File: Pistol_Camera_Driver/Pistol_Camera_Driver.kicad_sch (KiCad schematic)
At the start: 118 parts, among them J1 Screw_Terminal_01x02, J10 I2C, J11 Screw_Terminal_01x02, J12 Screw_Terminal_01x02, J13 I2C, J14 Screw_Terminal_01x02, J15 Screw_Terminal_01x02, J16 Screw_Terminal_01x02, J17 Screw_Terminal_01x02, J19 I2C, J2 Objective, J3 Screw_Terminal_01x02, J4 Screw_Terminal_01x02, J5 Screw_Terminal_01x02, J6 Joystick, J7 Screw_Terminal_01x02, J8 Screw_Terminal_01x02, J9 Screw_Terminal_01x02, M1 Fan, U1 XL1509-3.3, U12 MT3608, U2 XL1509-5.0, U4 DRV8834PWP, U5 DRV8834PWP

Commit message: v0.2 circuit was completed
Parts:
- removed C20, C22: 22u, Capacitor_SMD:C_0603_1608Metric_Pad1.08x0.95mm_HandSolder, symbol Device:C
- removed C21, C24: 0.1, Capacitor_SMD:C_0603_1608Metric_Pad1.08x0.95mm_HandSolder, symbol Device:C
- removed D1, D9: UV_LED, symbol Device:LED
- removed D2, D4, D6: CDBA3100-HF, Diode_SMD:D_SMA, symbol Diode:CDBA3100-HF
- removed D3: WHITE_LED, symbol Device:LED
- removed D5: RED_LED, symbol Device:LED
- removed R14, R15, R16, R18, R20, R21, R22, R23, R24, R25, R26, R27, R28, R29, R30, R31, R32, R33, R34, R35, R36, R37, R38, R39: 1, Resistor_SMD:R_0603_1608Metric_Pad0.98x0.95mm_HandSolder, symbol Device:R
- removed U6, U7, U8, U9: ~, Package_SO:PowerIntegrations_SO-8, symbol Vedro:LED2000DR
- added R42, R43, R44, R45: 10k, Resistor_SMD:R_0603_1608Metric_Pad0.98x0.95mm_HandSolder, symbol Device:R
- added R46, R47, R48, R49, R52, R53, R54, R55: 1, Resistor_SMD:R_0603_1608Metric_Pad0.98x0.95mm_HandSolder, symbol Device:R
- added U11, U13, U14, U15: ~, Package_TO_SOT_SMD:SOT-89-5_Handsoldering, symbol myLib8_sym:BP1361
- added VD1, VD2, VD3, VD4, VD5, VD6, VD7: CDBA3100-HF, Diode_SMD:D_SOD-123, symbol Diode:CDBA3100-HF
- C13, C15, C16, C17, C19, C3: footprint Capacitor_SMD:C_0603_1608Metric_Pad1.08x0.95mm_HandSolder -> Capacitor_SMD:C_0805_2012Metric_Pad1.18x1.45mm_HandSolder
- C14, C18: value 0.1 -> 22u; footprint Capacitor_SMD:C_0603_1608Metric_Pad1.08x0.95mm_HandSolder -> Capacitor_SMD:C_0805_2012Metric_Pad1.18x1.45mm_HandSolder
- L1, L2, L3, L4: value 4u7 -> 47uH; footprint Inductor_SMD:L_Chilisin_BMRx00040412 -> Inductor_SMD:L_APV_ANR5045
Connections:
- net +3.3VP: now also VD7.1 (K)
- net +5V: now also VD6.1 (K)
- net EP: now also C17.1, C19.1, C3.1, R42.2, R43.2, R44.2, R45.2, U11.2 (GND), U13.2 (GND), U14.2 (GND), U15.2 (GND), VD6.2 (A), VD7.2 (A); no longer C13.2, C15.2, C16.2, C17.2, C18.1, C19.2, C3.2
- net PWM_IR: now also R45.1, U15.3 (DIM)
- net PWM_RED: now also R43.1, U13.3 (DIM)
- net PWM_UV: now also R44.1, U14.3 (DIM)
- net PWM_WHITE: now also R42.1, U11.3 (DIM)
- net VPP: now also C17.2, C19.2, C3.2, R46.1, R47.1, R48.1, R49.1, R52.1, R53.1, R54.1, R55.1, U11.5 (VIN), U13.5 (VIN), U14.1 (CS), U14.5 (VIN), U15.5 (VIN), VD1.1 (K), VD2.1 (K), VD3.1 (K), VD4.1 (K), VD5.1 (K); no longer C15.1, C16.1, C18.2, C19.1
- net at J12.2 (Pin_2): now also C18.2, L2.2
- net at L2.1: now also U15.4 (SW), VD4.2 (A)
- net at Je1.2 (Pin_2): now also C13.2, L4.2
- net at J9.2 (Pin_2): now also C16.2, L3.2
- net at L4.1: now also U11.4 (SW), VD1.2 (A)
- net at J12.1 (Pin_1): now also C18.1, R54.2, R55.2, U15.1 (CS); no longer L4.2
- net at L7.2, U12.1 (SW): now also VD5.2 (A)
- net at J7.2 (Pin_2): now also C15.2, L1.2
- net at L1.1: now also U13.4 (SW), VD2.2 (A)
- net at L3.1: now also U14.4 (SW), VD3.2 (A)
- new net: C13.1, Je1.1 (Pin_1), R46.2, R47.2, U11.1 (CS)
- new net: C16.1, J9.1 (Pin_1), R52.2, R53.2
- new net: C15.1, J7.1 (Pin_1), R48.2, R49.2, U13.1 (CS)

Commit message: v0.3 actual state
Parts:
- removed C23: 470uF, Capacitor_SMD:CP_Elec_10x10.5, symbol Device:C_Polarized
- removed C26: 180uF, Capacitor_SMD:CP_Elec_6.3x7.7, symbol Device:C_Polarized
- removed Je1: Screw_Terminal_01x02, Connector_PinSocket_2.54mm:PinSocket_1x02_P2.54mm_Vertical, symbol Connector:Screw_Terminal_01x02
- removed U13, U14, U15: ~, Package_TO_SOT_SMD:SOT-89-5_Handsoldering, symbol myLib8_sym:BP1361
- added C20: 470uF, Capacitor_THT:CP_Radial_D8.0mm_P3.50mm, symbol Device:C_Polarized
- added C21: 330uF, Capacitor_THT:CP_Radial_D8.0mm_P3.50mm, symbol Device:C_Polarized
- added J18: Screw_Terminal_01x02, Connector_JST:JST_XH_B2B-XH-A_1x02_P2.50mm_Vertical, symbol Connector:Screw_Terminal_01x02
- added R14, R15, R16, R18, R20, R21, R22, R23, R24, R25, R26, R27, R28, R29, R30, R31: 1, Resistor_SMD:R_0603_1608Metric_Pad0.98x0.95mm_HandSolder, symbol Device:R
- added U6, U7, U8: ~, Package_TO_SOT_SMD:SOT-89-5, symbol myLib8_sym:BP1361
- C4: footprint Capacitor_SMD:CP_Elec_10x10.5 -> Capacitor_THT:CP_Radial_D8.0mm_P3.50mm
- C6: value 180uF -> 330uF; footprint Capacitor_SMD:CP_Elec_6.3x7.7 -> Capacitor_THT:CP_Radial_D8.0mm_P3.50mm
- J1, J12, J14, J15, J16, J17, J3, J4, J5, J7, J8, J9: footprint Connector_PinSocket_2.54mm:PinSocket_1x02_P2.54mm_Vertical -> Connector_JST:JST_XH_B2B-XH-A_1x02_P2.50mm_Vertical
- J6: footprint Connector_PinSocket_2.54mm:PinSocket_1x05_P2.54mm_Vertical -> Connector_JST:JST_XH_B5B-XH-A_1x05_P2.50mm_Vertical
- U11: footprint Package_TO_SOT_SMD:SOT-89-5_Handsoldering -> Package_TO_SOT_SMD:SOT-89-5
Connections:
- net +5V: now also C21.1
- net EP: now also C20.2, C21.2, U6.2 (GND), U7.2 (GND), U8.2 (GND)
- net PWM_IR: now also U8.3 (DIM)
- net PWM_RED: now also U6.3 (DIM)
- net PWM_UV: now also U7.3 (DIM)
- net VPP: now also C20.1, R14.1, R15.1, R16.1, R18.1, R20.1, R21.1, R22.1, R23.1, R24.1, R25.1, R26.1, R27.1, R28.1, R29.1, R30.1, R31.1, U6.5 (VIN), U7.5 (VIN), U8.5 (VIN)
- net at C13.1, R46.2, R47.2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: now also J18.1 (Pin_1), R28.2, R29.2, R30.2, R31.2
- net at C13.2, L4.2: now also J18.2 (Pin_2)
- net at L2.1, VD4.2 (A): now also U8.4 (SW)
- net at C18.1, J12.1 (Pin_1), R54.2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: now also R14.2, R15.2, R16.2, R18.2, U8.1 (CS)
- net at C16.1, J9.1 (Pin_1), R52.2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: now also R20.2, R21.2, R22.2, R23.2, U7.1 (CS)
- net at L3.1, VD3.2 (A): now also U7.4 (SW)
- net at C15.1, J7.1 (Pin_1), R48.2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: now also R24.2, R25.2, R26.2, R27.2, U6.1 (CS)
- net at L1.1, VD2.2 (A): now also U6.4 (SW)
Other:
- moved on the sheet: C14, M1

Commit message: v0.4 draft decomposition completed
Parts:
- removed J10: I2C, Connector_JST:JST_XH_B4B-XH-A_1x04_P2.50mm_Vertical, symbol Connector:Conn_01x04_Female
- removed R18, R20, R21, R23, R24, R25, R26, R27, R28, R29, R30, R31, R46, R47, R48, R49, R52, R53, R54, R55: 1, Resistor_SMD:R_0603_1608Metric_Pad0.98x0.95mm_HandSolder, symbol Device:R
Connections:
- net at C16.1, J9.1 (Pin_1), U7.1 (CS): now also R15.2; no longer R22.2
- net at C13.1, J18.1 (Pin_1), U11.1 (CS): now also R14.2
- net at C15.1, J7.1 (Pin_1), U6.1 (CS): now also R16.2
- net at C18.1, J12.1 (Pin_1), U8.1 (CS): now also R22.2; no longer R14.2, R15.2, R16.2

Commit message: v0.6 actual state
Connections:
- net PWM_IR: now also R42.1, U11.3 (DIM); no longer R45.1, U8.3 (DIM)
- net PWM_WHITE: now also R45.1, U8.3 (DIM); no longer R42.1, U11.3 (DIM)

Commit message: v0.7 draft routung completed
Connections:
- net +3.3VP: now also R1.1, R13.1, R8.1
- net +3V3: no longer R1.1, R13.1, R8.1
- net K3: now also J17.1 (Pin_1); no longer J14.1 (Pin_1)
- net K4: now also J16.1 (Pin_1); no longer J15.1 (Pin_1)
- net K5: now also J15.1 (Pin_1); no longer J16.1 (Pin_1)
- net K6: now also J14.1 (Pin_1); no longer J17.1 (Pin_1)

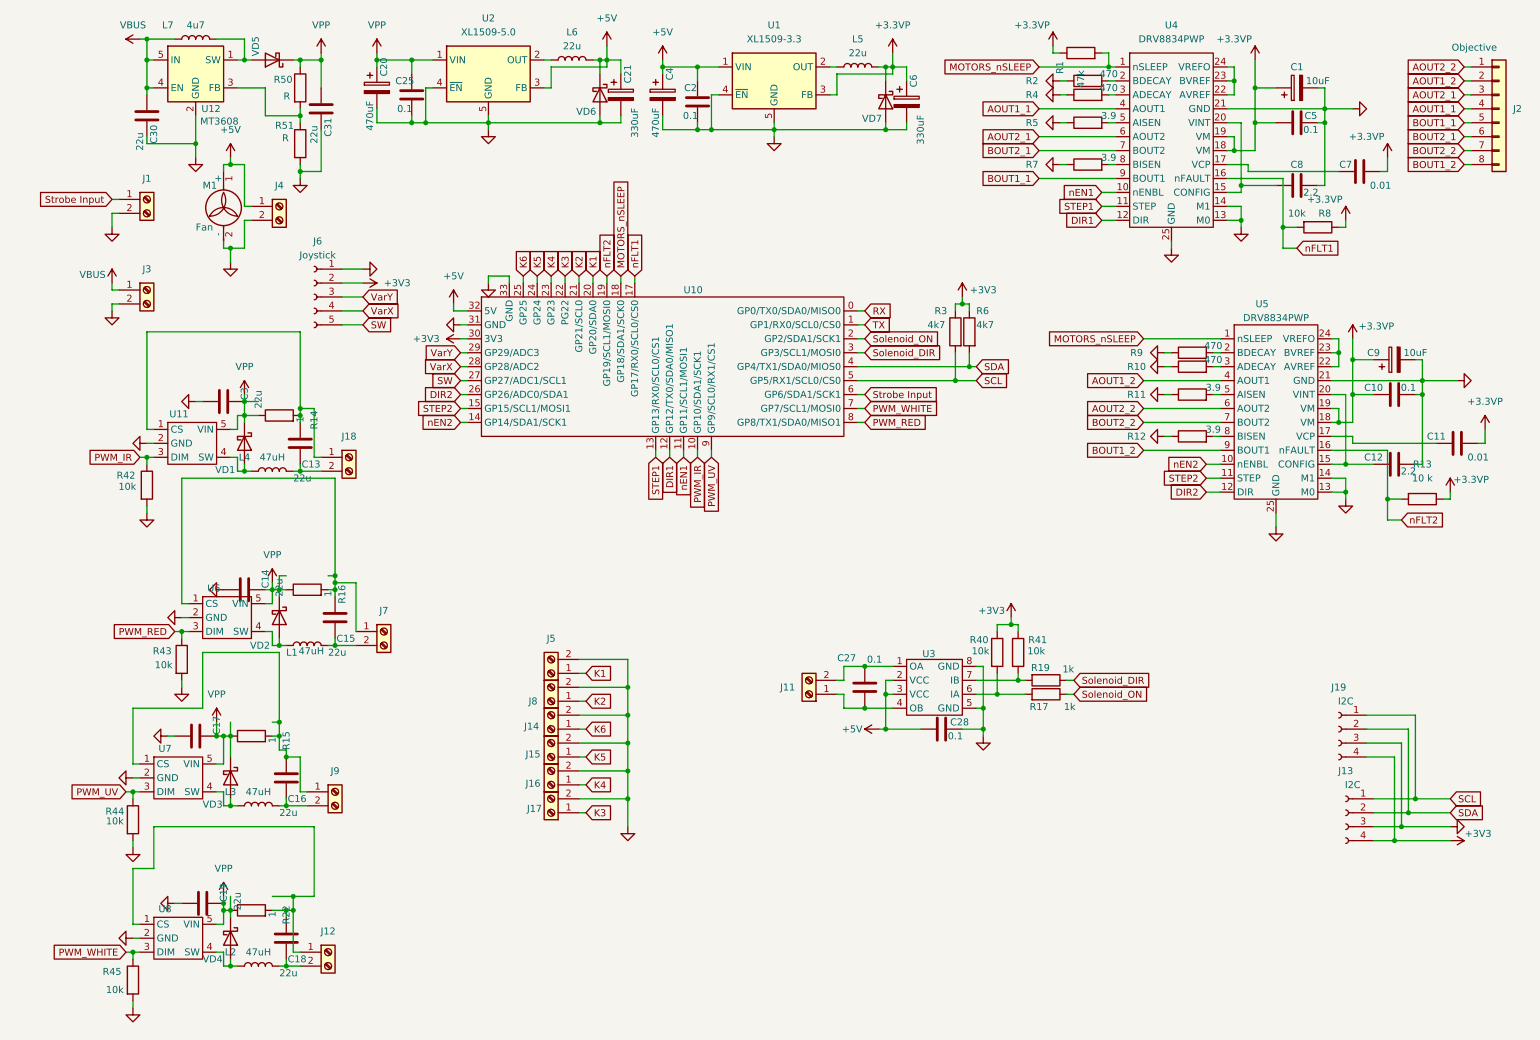
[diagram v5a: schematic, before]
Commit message: v0.8 compact BUCK converter for 3v3 was added
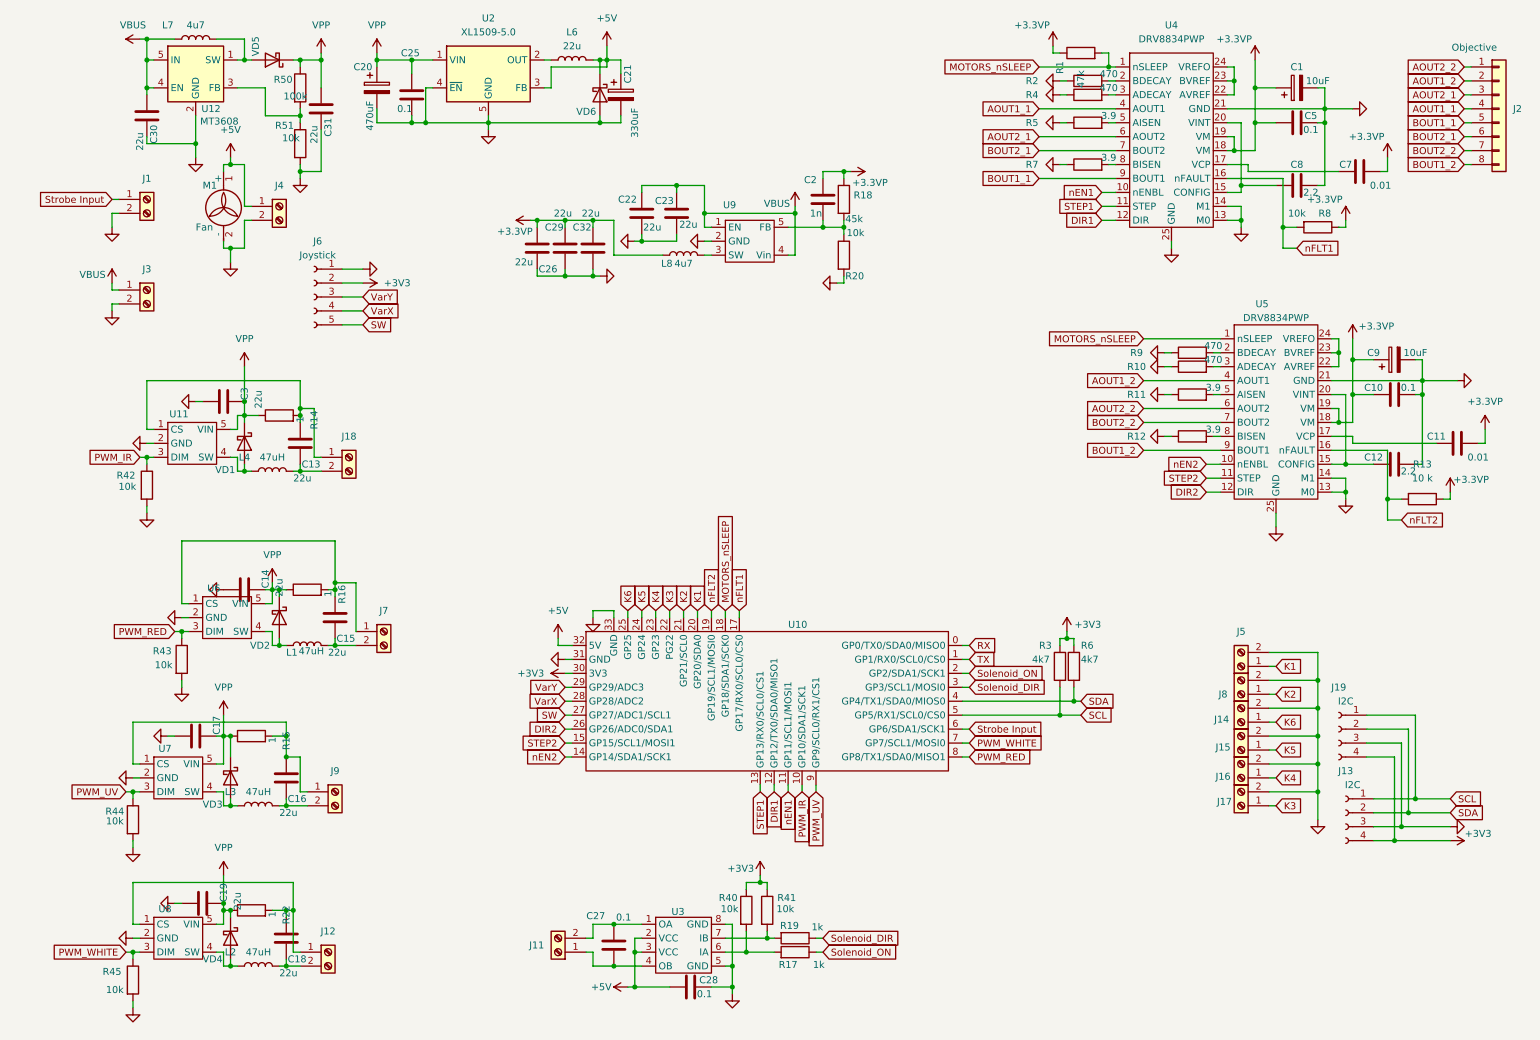
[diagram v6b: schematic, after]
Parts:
- removed C4: 470uF, Capacitor_THT:CP_Radial_D8.0mm_P3.50mm, symbol Device:C_Polarized
- removed C6: 330uF, Capacitor_THT:CP_Radial_D8.0mm_P3.50mm, symbol Device:C_Polarized
- removed L5: 22u, Inductor_SMD:L_Sunlord_SWPA4012S, symbol Device:L
- removed U1: XL1509-3.3, Package_SO:SOIC-8-1EP_3.9x4.9mm_P1.27mm_EP2.95x4.9mm_Mask2.71x3.4mm_ThermalVias, symbol Vedro:XL1509-3.3
- removed VD7: CDBA3100-HF, Diode_SMD:D_SOD-123, symbol Diode:CDBA3100-HF
- added C22, C23, C26, C29, C32: 22u, Capacitor_SMD:C_0805_2012Metric_Pad1.18x1.45mm_HandSolder, symbol Device:C
- added L8: 4u7, Inductor_SMD:L_Chilisin_BMRx00040412, symbol Device:L
- added R18: 45k, Resistor_SMD:R_0603_1608Metric_Pad0.98x0.95mm_HandSolder, symbol Device:R
- added R20: 10k, Resistor_SMD:R_0603_1608Metric_Pad0.98x0.95mm_HandSolder, symbol Device:R
- added U9: ~, Package_TO_SOT_SMD:SOT-23-5, symbol myLib8_sym:RY3430
- C2: value 0.1 -> 1n
- R50: value R -> 100k
- R51: value R -> 10k
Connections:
- net +3.3VP: now also C2.1, C26.1, C29.2, C32.2, L8.1, R18.1
- net +5V: no longer C2.1
- net VBUS: now also C22.1, C23.2, U9.1 (EN), U9.4 (Vin)
- net EP renamed GND
- net GND: now also C22.2, C23.1, C26.2, C29.1, C32.1, R20.2, U9.2 (GND); no longer C2.2
- new net: C2.2, R18.2, R20.1, U9.5 (FB)
- new net: L8.2, U9.3 (SW)
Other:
- moved on the sheet: C27, C28, J11, J14, J15, J16, J17, J5, J8, R17, R19, R3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

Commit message: v0.9 actual state
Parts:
- removed C20: 470uF, Capacitor_THT:CP_Radial_D8.0mm_P3.50mm, symbol Device:C_Polarized
- removed C21: 330uF, Capacitor_THT:CP_Radial_D8.0mm_P3.50mm, symbol Device:C_Polarized
- removed C25: 0.1, Capacitor_SMD:C_0603_1608Metric_Pad1.08x0.95mm_HandSolder, symbol Device:C
- removed L6: 22u, Inductor_SMD:L_Sunlord_SWPA4012S, symbol Device:L
- removed U2: XL1509-5.0, Package_SO:SOIC-8-1EP_3.9x4.9mm_P1.27mm_EP2.95x4.9mm_Mask2.71x3.4mm_ThermalVias, symbol Regulator_Switching:XL1509-5.0
- removed VD6: CDBA3100-HF, Diode_SMD:D_SOD-123, symbol Diode:CDBA3100-HF
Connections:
- net +3.3VP: now also C28.2, U3.2 (VCC), U3.3 (VCC)
- net VBUS: now also J4.1 (Pin_1), M1.1 (+), U10.32 (5V)
- removed net +5V: C28.2, J4.1 (Pin_1), M1.1 (+), U10.32 (5V), U3.2 (VCC), U3.3 (VCC)
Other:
- moved on the sheet: R15

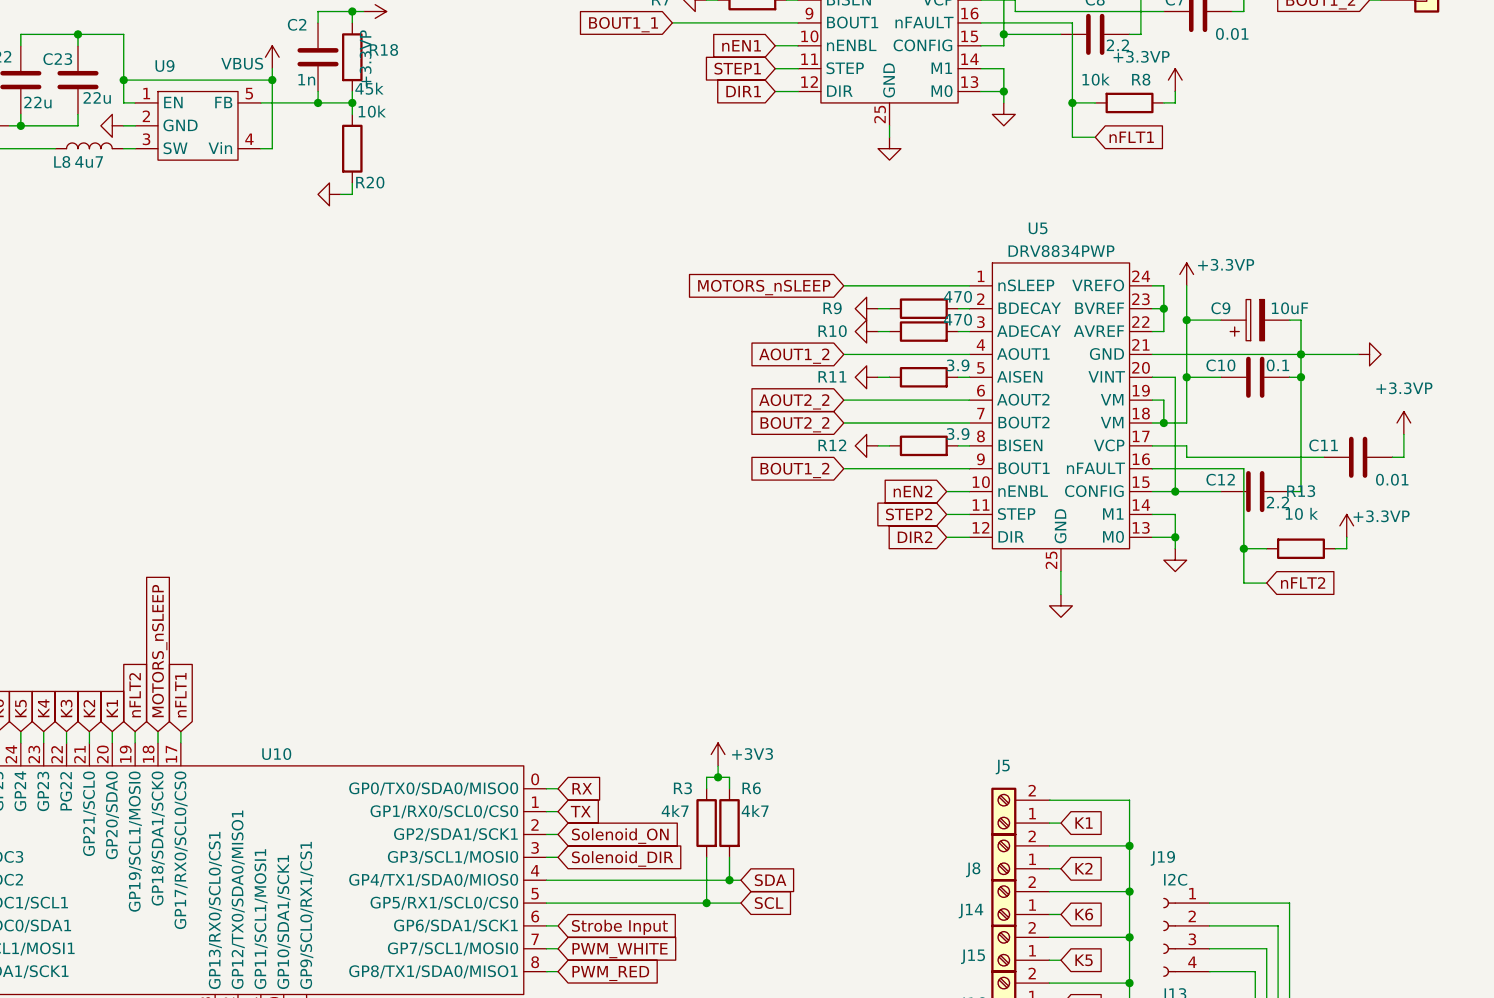
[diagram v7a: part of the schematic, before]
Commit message: v1.0 Draft routing and DRC completed
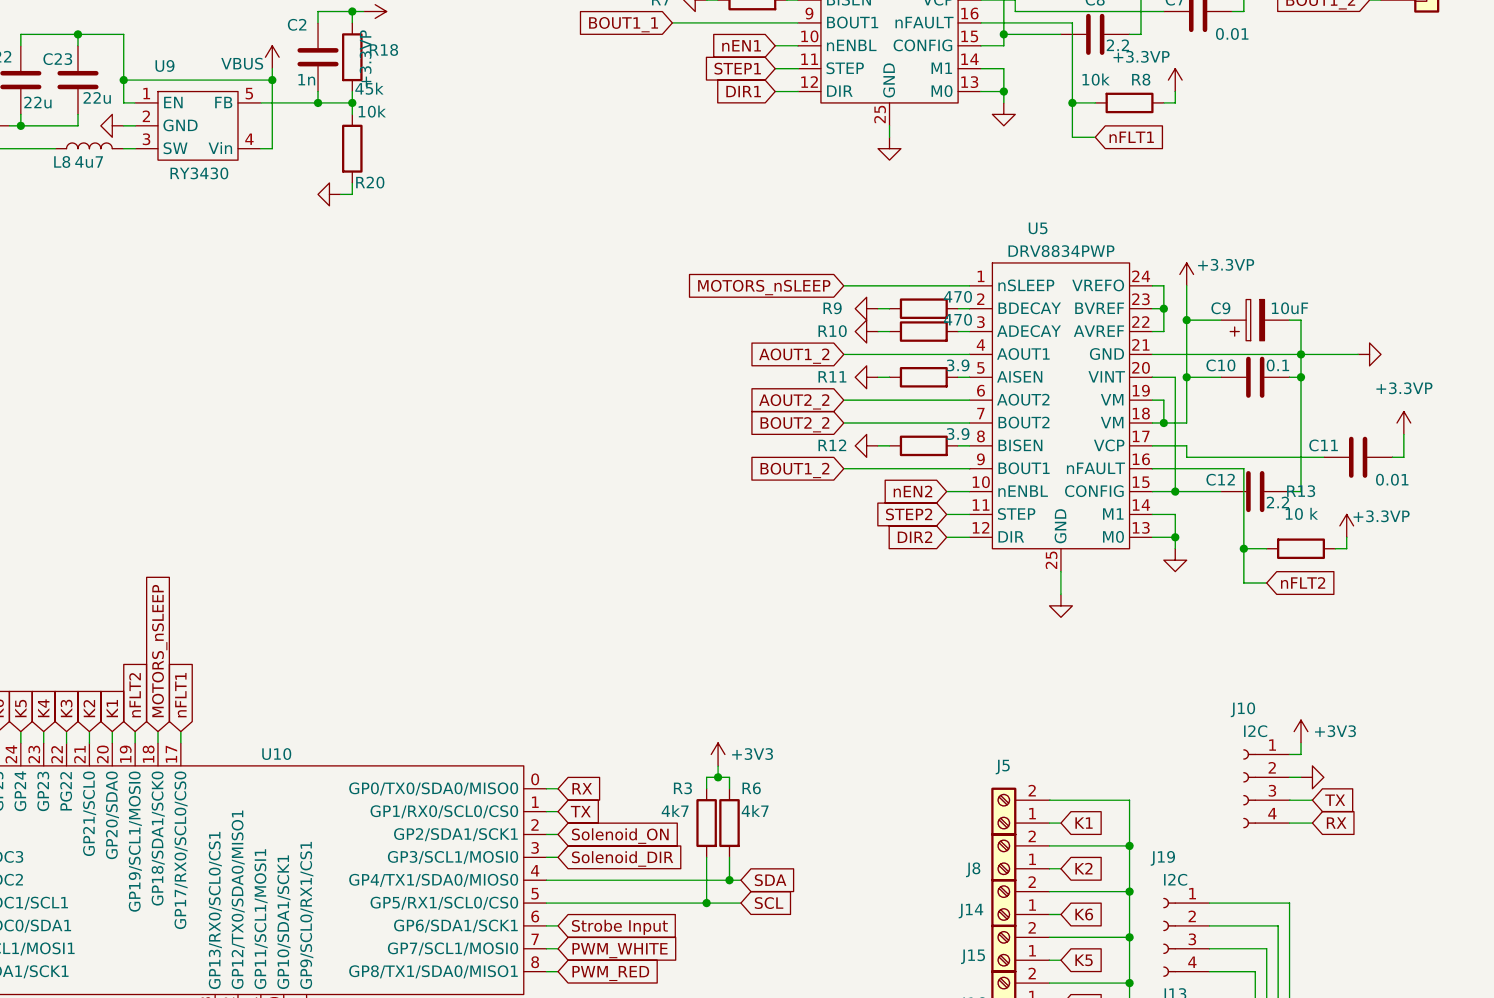
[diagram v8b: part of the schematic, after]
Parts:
- added J10: I2C, Connector_PinSocket_2.54mm:PinSocket_1x04_P2.54mm_Vertical, symbol Connector:Conn_01x04_Female
- C1, C9: footprint Capacitor_THT:CP_Radial_D6.3mm_P2.50mm -> Capacitor_THT:CP_Radial_D5.0mm_P2.00mm
- U9: value ~ -> RY3430
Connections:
- net +3V3: now also J10.1 (Pin_1)
- net GND: now also J10.2 (Pin_2)
- net RX: now also J10.4 (Pin_4)
- net TX: now also J10.3 (Pin_3)
